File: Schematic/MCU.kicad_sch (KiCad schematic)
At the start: 0 parts

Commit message: Started to work on the BOM
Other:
- sheet ESP32 ports: added none; removed BMP_INT, GPS_RX, GPS_TX, IMU_INT, IMU_nRESET
- sheet External 40 Pin Header ports: added none; removed SENSOR_P3V3
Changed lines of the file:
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@@
-	(wire
-		(pts
-			(xy 228.6 43.18) (xy 248.92 43.18)
-		)
-		(stroke
-			(width 0)
-			(type default)
-		)
-	)
 	(wire
 		(pts
@@
 	(wire
 		(pts
-			(xy 165.1 40.64) (xy 185.42 40.64)
-		)
-		(stroke
-			(width 0)
-			(type default)
-		)
-	)
-	(wire
-		(pts
-			(xy 165.1 44.45) (xy 185.42 44.45)
+			(xy 168.91 40.64) (xy 185.42 40.64)
 		)
 		(stroke
@@
 	(wire
 		(pts
-			(xy 165.1 72.39) (xy 185.42 72.39)
-		)
-		(stroke
-			(width 0)
-			(type default)
-		)
-	)
-	(wire
-		(pts
 			(xy 165.1 60.96) (xy 185.42 60.96)
 		)
@@
 	(wire
 		(pts
-			(xy 165.1 82.55) (xy 185.42 82.55)
-		)
-		(stroke
-			(width 0)
-			(type default)
-		)
-	)
-	(wire
-		(pts
 			(xy 165.1 53.34) (xy 185.42 53.34)
 		)
@@
 	(wire
 		(pts
-			(xy 58.42 92.71) (xy 82.55 92.71)
-		)
-		(stroke
-			(width 0)
-			(type default)
-		)
-	)
-	(wire
-		(pts
 			(xy 119.38 45.72) (xy 139.7 45.72)
 		)
@@
 		(pts
 			(xy 228.6 45.72) (xy 248.92 45.72)
-		)
-		(stroke
-			(width 0)
-			(type default)
-		)
-	)
-	(wire
-		(pts
-			(xy 165.1 46.99) (xy 185.42 46.99)
 		)
 		(stroke
@@
 		)
 	)
-	(label "IMU_INT"
-		(at 165.1 72.39 0)
-		(effects
-			(font
-				(size 1.27 1.27)
-			)
-			(justify left bottom)
-		)
-	)
 	(label "IO_RST"
 		(at 248.92 45.72 180)
@@
 		)
 	)
-	(label "GPS_RX"
-		(at 165.1 44.45 0)
-		(effects
-			(font
-				(size 1.27 1.27)
-			)
-			(justify left bottom)
-		)
-	)
-	(label "BMP_INT"
-		(at 165.1 82.55 0)
-		(effects
-			(font
-				(size 1.27 1.27)
-			)
-			(justify left bottom)
-		)
-	)
 	(label "MOTOR_PH_DATA"
 		(at 165.1 91.44 0)
@@
 		)
 	)
-	(label "IMU_nRESET"
-		(at 248.92 43.18 180)
-		(effects
-			(font
-				(size 1.27 1.27)
-			)
-			(justify right bottom)
-		)
-	)
 	(label "I2C_SDA"
 		(at 62.23 105.41 0)
@@
 		)
 	)
-	(label "GPS_TX"
-		(at 165.1 46.99 0)
-		(effects
-			(font
-				(size 1.27 1.27)
-			)
-			(justify left bottom)
-		)
-	)
 	(label "SPI_SDO"
 		(at 62.23 115.57 0)
@@
 	)
 	(label "SENSOR_P3V3"
-		(at 165.1 40.64 0)
+		(at 168.91 40.64 0)
 		(effects
 			(font
@@
 			)
 			(justify right bottom)
-		)
-	)
-	(label "SENSOR_P3V3"
-		(at 62.23 92.71 0)
-		(effects
-			(font
-				(size 1.27 1.27)
-			)
-			(justify left bottom)
 		)
 	)
@@
 		)
 	)
-	(hierarchical_label "SENSOR_P3V3"
-		(shape input)
-		(at 58.42 92.71 180)
-		(effects
-			(font
-				(size 1.27 1.27)
-			)
-			(justify right)
-		)
-	)
 	(hierarchical_label "ENCODER_SEL2"
 		(shape output)
@@
 		(shape input)
 		(at 58.42 120.65 180)
+		(effects
+			(font
+				(size 1.27 1.27)
+			)
+			(justify right)
+		)
+	)
+	(hierarchical_label "SENSOR_P3V3"
+		(shape input)
+		(at 168.91 40.64 180)
 		(effects
 			(font
@@
 		(size 38.1 54.61)
 		(exclude_from_sim no)
-		(in_bom yes)
-		(on_board yes)
-		(dnp no)
+		(in_bom no)
+		(on_board no)
+		(dnp yes)
 		(fields_autoplaced yes)
 		(stroke
@@
 				)
 				(justify right)
-			)
-		)
-		(pin "SENSOR_P3V3" input
-			(at 82.55 92.71 180)
-			(effects
-				(font
-					(size 1.27 1.27)
-				)
-				(justify left)
 			)
 		)
@@
 			)
 		)
-		(pin "IMU_nRESET" output
-			(at 228.6 43.18 0)
-			(effects
-				(font
-					(size 1.27 1.27)
-				)
-				(justify right)
-			)
-		)
-		(pin "BMP_INT" input
-			(at 185.42 82.55 180)
-			(effects
-				(font
-					(size 1.27 1.27)
-				)
-				(justify left)
-			)
-		)
 		(pin "ENCODER_SEL1" output
 			(at 228.6 57.15 0)
@@
 			)
 		)
-		(pin "GPS_RX" input
-			(at 185.42 44.45 180)
-			(effects
-				(font
-					(size 1.27 1.27)
-				)
-				(justify left)
-			)
-		)
-		(pin "GPS_TX" output
-			(at 185.42 46.99 180)
-			(effects
-				(font
-					(size 1.27 1.27)
-				)
-				(justify left)
-			)
-		)
 		(pin "I2C_SCL" output
 			(at 185.42 50.8 180)
@@
 			(effects
 				(font
-					(size 1.27 1.27)
-				)
-				(justify left)
-			)
-		)
-		(pin "IMU_INT" input
-			(at 185.42 72.39 180)
-			(effects
-				(font

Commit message: Massive pivit, simplification
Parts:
- added C1, C13, C20, C23, C25, C26, C27, C28, C29, C30, C9: 100n, symbol Device:C
- added C10, C11, C18, C4: 100n, Capacitor_SMD:C_1206_3216Metric_Pad1.33x1.80mm_HandSolder, symbol Device:C
- added C12: 470n, Capacitor_SMD:C_0805_2012Metric_Pad1.18x1.45mm_HandSolder, symbol Device:C
- added C14, C15: 10p, symbol Device:C
- added C16, C2, C3: 4u7, Capacitor_SMD:C_1206_3216Metric_Pad1.33x1.80mm_HandSolder, symbol Device:C
- added C17, C22: 1u, symbol Device:C
- added C19, C21: 2u2, symbol Device:C
- added C24: 4u7, symbol Device:C
- added C31, C32: 12p, symbol Device:C
- added C5, C6, C7, C8: 10n, Capacitor_SMD:C_1206_3216Metric_Pad1.33x1.80mm_HandSolder, symbol Device:C
- added D1, D2, D3, D4, D7: 82306050029, 82306050029:WESURGE_0603134, symbol 82306050029:82306050029
- added D5: BLUE, ASMM-CR03-BU802:LEDM3528X210N, symbol PCM_SL_Devices:LED
- added D6: RED, ASMM-CR03-BU802:LEDM3528X210N, symbol PCM_SL_Devices:LED
- added FB1: 21R, symbol Device:FerriteBead_Small
- added FB2: 1k, symbol Device:FerriteBead_Small
- added J7: USB_C_Receptacle_USB2.0_14P, symbol Connector:USB_C_Receptacle_USB2.0_14P
- added J8: Conn_01x04, symbol Connector_Generic:Conn_01x04
- added NT1: NetTie_2, symbol Device:NetTie_2
- added Q1: PDTC114ET,215, PDTC114ET,215:SOT95P230X110-3N, symbol PDTC114ET,215:PDTC114ET,215
- added R1: 100k, symbol Device:R
- added R10, R13, R5: 330R, symbol Device:R
- added R11, R12: 22R, symbol Device:R
- added R2, R3: 5k1, symbol Device:R
- added R4, R7: 1k5, symbol Device:R
- added R6: 500R, symbol Device:R
- added R8: 10k, symbol Device:R
- added R9: 0R, symbol Device:R
- added SW3, SW4, SW5: SW_MEC_5E, T6VJ11GQR:T6VJ11GQR, symbol Switch:SW_MEC_5E
- added TP12, TP13, TP14, TP15, TP16, TP17, TP18: TestPoint, symbol Connector:TestPoint
- added U1: MAX809TEUR+T, MAX809TEUR+T:SOT95P237X112-3N, symbol MAX809TEUR+T:MAX809TEUR+T
- added U2: TVS2200DRV, symbol Power_Protection:TVS2200DRV
- added U3: TPS2115ADRBT, symbol TPS2115ADRBT:TPS2115ADRBT
- added U4: LM3940ISX-3.3/NOPB, symbol LM3940ISX-3-3-NOPB:LM3940ISX-3.3_NOPB
- added U5: STM32H743VIT6, Package_QFP:LQFP-100_14x14mm_P0.5mm, symbol MCU_ST_STM32H7:STM32H743VITx
- added Y1: 25M 10pF, symbol Device:Crystal_Small
- added Y2: 32.768k 7pF, symbol Device:Crystal_Small
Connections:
- net MCU_VBUS: now also C11.1, C2.2, C3.2, C4.2, FB1.2, TP12.1, U3.8 (IN1)
- net USB_C_N: now also D2.1 (A1), J7.A7 (D-), J7.B7 (D-), TP15.1
- net USB_C_P: now also D3.1 (A1), J7.A6 (D+), J7.B6 (D+), TP16.1
- new net: R1.1, R4.1, U1.2 (~{RESET})
- new net: C14.2, U5.12 (PH0), Y1.2
- new net: J8.3 (Pin_3), R12.2
- new net: C15.2, U5.13 (PH1), Y1.1
- new net: C5.1, C6.1, C7.1, C8.1, FB1.1, J7.A4 (VBUS), J7.A9 (VBUS), J7.B4 (VBUS), J7.B9 (VBUS), U2.4 (IN), U2.5 (IN), U2.6 (IN)
- new net: C32.1, U5.9 (PC15), Y2.1
- new net: C31.1, U5.8 (PC14), Y2.2
- new net: D5.1, Q1.3 (C)
- new net: D5.2, R7.2
- new net: J8.2 (Pin_2), R11.2
- new net: Q1.1 (B), U5.2 (PE3)
- new net: C19.1, U5.48 (VCAP)
- new net: R13.1, U5.7 (PC13)
- new net: C21.1, U5.73 (VCAP)
- new net: R6.1, U3.4 (ILIM)
- new net: D6.2, R10.2
- new net: C12.1, TP17.1, U3.7 (OUT), U4.1 (IN)
- new net: D7.1 (A1), R13.2, SW5.1, SW5.2
- new net BOOT0: D1.1 (A1), R8.2, SW3.1, SW3.2, U5.94 (BOOT0)
- new net C_CC1: J7.A5 (CC1), R2.1, TP13.1
- new net C_CC2: J7.B5 (CC2), R3.1, TP14.1
- new net GND: C1.2, C10.2, C11.2, C12.2, C13.1, C14.1, C15.1, C16.2, C17.2, C18.2, C19.2, C2.1, C20.2, C21.2, C22.2, C23.2, C24.2, C25.2, C26.2, C27.2, C28.2, C29.2, C3.1, C30.2, C31.2, C32.2, C4.1, C5.2, C6.2, C7.2, C8.2, C9.2, D1.2 (A2), D2.2 (A2), D3.2 (A2), D4.2 (A2), D6.1, D7.2 (A2), J7.A1 (GND), J7.A12 (GND), J7.B1 (GND), J7.B12 (GND), J7.S1 (SHIELD), J8.4 (Pin_4), NT1.1, Q1.2 (E), R1.2, R2.2, R3.2, R6.2, R8.1, SW4.3 (K), SW4.4 (A), U1.1 (GND), U2.1 (GND), U2.2 (GND), U2.3 (GND), U2.7 (GND), U3.3 (D1), U3.5 (GND), U3.9 (EPAD), U4.2 (GND), U5.10 (VSS), U5.26 (VSS), U5.49 (VSS), U5.74 (VSS), U5.99 (VSS)
- new net MCU_P3V3: C1.1, C16.1, C18.1, C24.1, C25.1, C26.1, C27.1, C28.1, C29.1, C30.1, FB2.1, J8.1 (Pin_1), R10.1, R7.1, SW3.3 (K), SW3.4 (A), SW5.3 (K), SW5.4 (A), TP18.1, U1.3 (VCC), U4.3 (OUT), U5.100 (VDD), U5.11 (VDD), U5.27 (VDD), U5.50 (VDD), U5.6 (VBAT), U5.75 (VDD)
- new net NRST: C13.2, D4.1 (A1), R4.2, SW4.1, SW4.2, U5.14 (NRST)
- new net P5V0: C10.1, U3.6 (IN2)
- new net SWCLK: R12.1, U5.76 (PA14)
- new net SWDIO: R11.1, U5.72 (PA13)
- new net SYS_RESET: C9.1, R5.2
- new net VDDA: C22.1, C23.1, FB2.2, R9.1, U5.21 (VDDA)
- new net VREF+: C17.1, C20.1, R9.2, U5.20 (VREF+)
- new net VSSA: NT1.2, U5.19 (VSSA)
- no-connect marks 0 -> 3
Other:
- removed sheet ESP32
- removed sheet External 40 Pin Header
- removed sheet MCU USB-C
- note added: "*** MAKE MORE THAN ONE AMP ***"
- note added: "100MHz"
- note added: "3V3 Line"
- note added: "3V3 Line 1A LDO"
- note added: "500/1A = 500"
- note added: "Auto-Switching Mode"
- note added: "Boot & Reset Buttons"
- note added: "Boot Switch"
- note added: "JTAG"
- note added: "Reset Switch"
- note added: "USB-C"
- note added: "User Button"

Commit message: now need 6V Line
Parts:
- removed C1, C13, C20, C23, C25, C26, C27, C28, C29, C30, C9: 100n, symbol Device:C
- removed C10, C11, C18, C4: 100n, Capacitor_SMD:C_1206_3216Metric_Pad1.33x1.80mm_HandSolder, symbol Device:C
- removed C12: 470n, Capacitor_SMD:C_0805_2012Metric_Pad1.18x1.45mm_HandSolder, symbol Device:C
- removed C14, C15: 10p, symbol Device:C
- removed C16, C2, C3: 4u7, Capacitor_SMD:C_1206_3216Metric_Pad1.33x1.80mm_HandSolder, symbol Device:C
- removed C17, C22: 1u, symbol Device:C
- removed C19, C21: 2u2, symbol Device:C
- removed C24: 4u7, symbol Device:C
- removed C31, C32: 12p, symbol Device:C
- removed C5, C6, C7, C8: 10n, Capacitor_SMD:C_1206_3216Metric_Pad1.33x1.80mm_HandSolder, symbol Device:C
- removed D1, D2, D3, D4, D7: 82306050029, 82306050029:WESURGE_0603134, symbol 82306050029:82306050029
- removed D5: BLUE, ASMM-CR03-BU802:LEDM3528X210N, symbol PCM_SL_Devices:LED
- removed D6: RED, ASMM-CR03-BU802:LEDM3528X210N, symbol PCM_SL_Devices:LED
- removed FB1: 21R, symbol Device:FerriteBead_Small
- removed FB2: 1k, symbol Device:FerriteBead_Small
- removed J7: USB_C_Receptacle_USB2.0_14P, symbol Connector:USB_C_Receptacle_USB2.0_14P
- removed J8: Conn_01x04, symbol Connector_Generic:Conn_01x04
- removed NT1: NetTie_2, symbol Device:NetTie_2
- removed Q1: PDTC114ET,215, PDTC114ET,215:SOT95P230X110-3N, symbol PDTC114ET,215:PDTC114ET,215
- removed R1: 100k, symbol Device:R
- removed R10, R13, R5: 330R, symbol Device:R
- removed R11, R12: 22R, symbol Device:R
- removed R2, R3: 5k1, symbol Device:R
- removed R4, R7: 1k5, symbol Device:R
- removed R6: 500R, symbol Device:R
- removed R8: 10k, symbol Device:R
- removed R9: 0R, symbol Device:R
- removed SW3, SW4, SW5: SW_MEC_5E, T6VJ11GQR:T6VJ11GQR, symbol Switch:SW_MEC_5E
- removed TP12, TP13, TP14, TP15, TP16, TP17, TP18: TestPoint, symbol Connector:TestPoint
- removed U1: MAX809TEUR+T, MAX809TEUR+T:SOT95P237X112-3N, symbol MAX809TEUR+T:MAX809TEUR+T
- removed U2: TVS2200DRV, symbol Power_Protection:TVS2200DRV
- removed U3: TPS2115ADRBT, symbol TPS2115ADRBT:TPS2115ADRBT
- removed U4: LM3940ISX-3.3/NOPB, symbol LM3940ISX-3-3-NOPB:LM3940ISX-3.3_NOPB
- removed U5: STM32H743VIT6, Package_QFP:LQFP-100_14x14mm_P0.5mm, symbol MCU_ST_STM32H7:STM32H743VITx
- removed Y1: 25M 10pF, symbol Device:Crystal_Small
- removed Y2: 32.768k 7pF, symbol Device:Crystal_Small
- added J14, J15: Conn_02x20_Odd_Even, symbol Connector_Generic:Conn_02x20_Odd_Even
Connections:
- net GND: now also J14.14 (Pin_14), J14.20 (Pin_20), J14.25 (Pin_25), J14.30 (Pin_30), J14.34 (Pin_34), J14.39 (Pin_39), J14.6 (Pin_6), J14.9 (Pin_9), J15.14 (Pin_14), J15.20 (Pin_20), J15.25 (Pin_25), J15.30 (Pin_30), J15.34 (Pin_34), J15.39 (Pin_39), J15.6 (Pin_6), J15.9 (Pin_9)
- net MCU_P3V3: now also J14.1 (Pin_1), J14.17 (Pin_17), J15.1 (Pin_1), J15.17 (Pin_17)
- new net 5V: J14.2 (Pin_2), J14.4 (Pin_4), J15.2 (Pin_2), J15.4 (Pin_4)
- new net ENCODER1_LFLAG/: J14.16 (Pin_16), J15.16 (Pin_16)
- new net ENCODER1_nCS: J14.15 (Pin_15), J15.15 (Pin_15)
- new net ENCODER2_LFLAG/: J14.18 (Pin_18), J15.18 (Pin_18)
- new net ENCODER2_nCS: J14.29 (Pin_29), J15.29 (Pin_29)
- new net GPCLK0: J14.7 (Pin_7), J15.7 (Pin_7)
- new net ID_SD: J14.27 (Pin_27), J15.27 (Pin_27)
- new net IO1: J14.28 (Pin_28), J15.28 (Pin_28)
- new net IO16: J14.36 (Pin_36), J15.36 (Pin_36)
- new net IO20: J14.38 (Pin_38), J15.38 (Pin_38)
- new net IO21: J14.40 (Pin_40), J15.40 (Pin_40)
- new net IO7: J14.26 (Pin_26), J15.26 (Pin_26)
- new net MOTOR1_EN_IN1: J14.32 (Pin_32), J15.32 (Pin_32)
- new net MOTOR1_PH_IN2: J14.31 (Pin_31), J15.31 (Pin_31)
- new net MOTOR1_nCS: J14.11 (Pin_11), J15.11 (Pin_11)
- new net MOTOR1_nFAULT: J14.22 (Pin_22), J15.22 (Pin_22)
- new net MOTOR2_EN_IN1: J14.33 (Pin_33), J15.33 (Pin_33)
- new net MOTOR2_PH_IN2: J14.37 (Pin_37), J15.37 (Pin_37)
- new net MOTOR2_nCS: J14.13 (Pin_13), J15.13 (Pin_13)
- new net MOTOR2_nFAULT: J14.24 (Pin_24), J15.24 (Pin_24)
- new net PCM_CLK: J14.12 (Pin_12), J15.12 (Pin_12)
- new net PCM_FS: J14.35 (Pin_35), J15.35 (Pin_35)
- new net RXD: J14.10 (Pin_10), J15.10 (Pin_10)
- new net SCL: J14.5 (Pin_5), J15.5 (Pin_5)
- new net SDA: J14.3 (Pin_3), J15.3 (Pin_3)
- new net SPI_SCLK: J14.23 (Pin_23), J15.23 (Pin_23)
- new net SPI_SDI: J14.19 (Pin_19), J15.19 (Pin_19)
- new net SPI_SDO: J14.21 (Pin_21), J15.21 (Pin_21)
- new net TXD: J14.8 (Pin_8), J15.8 (Pin_8)
- no-connect marks 3 -> 0
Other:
- note added: "FEMALE"
- note added: "MALE"
- note removed: "*** MAKE MORE THAN ONE AMP ***"
- note removed: "100MHz"
- note removed: "3V3 Line"
- note removed: "3V3 Line 1A LDO"
- note removed: "500/1A = 500"
- note removed: "Auto-Switching Mode"
- note removed: "Boot & Reset Buttons"
- note removed: "Boot Switch"
- note removed: "JTAG"
- note removed: "Reset Switch"
- note removed: "USB-C"
- note removed: "User Button"

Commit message: bom progress
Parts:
- J14: footprint (none) -> 7-534206-0:SHDR40W69P254_2X20_5080X503X813P
- J15: footprint (none) -> Connector_PinHeader_2.54mm:PinHeader_2x20_P2.54mm_Vertical
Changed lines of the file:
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@@
 			)
 		)
-		(property "Footprint" ""
+		(property "Footprint" "Connector_PinHeader_2.54mm:PinHeader_2x20_P2.54mm_Vertical"
 			(at 196.85 96.52 0)
 			(effects
@@
 			)
 		)
-		(property "Footprint" ""
+		(property "Footprint" "7-534206-0:SHDR40W69P254_2X20_5080X503X813P"
 			(at 96.52 96.52 0)
 			(effects

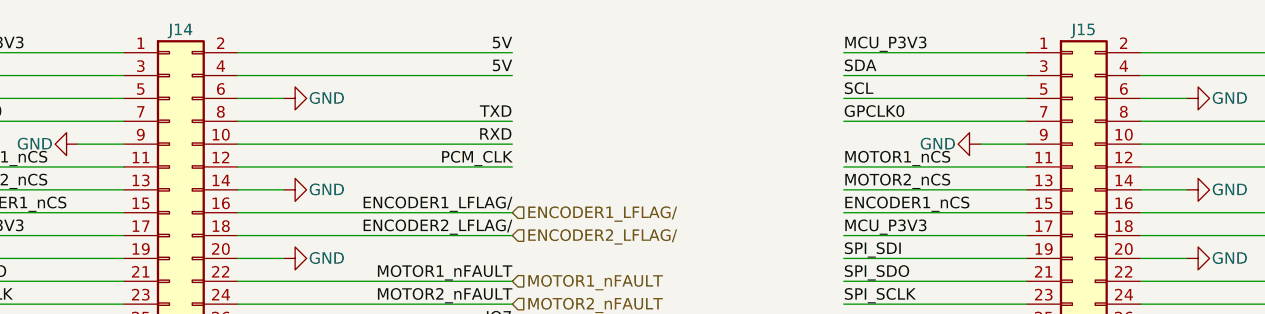
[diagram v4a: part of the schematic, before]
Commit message: added test points and fet
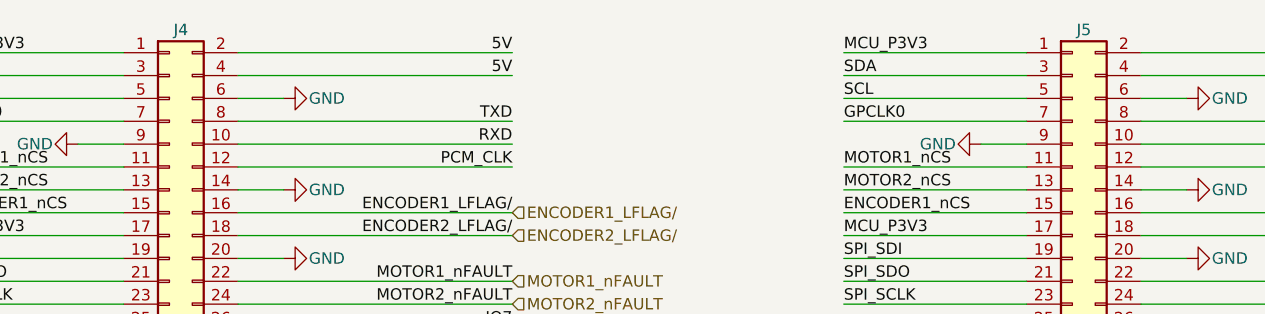
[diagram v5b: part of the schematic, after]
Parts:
- renumbered J14 to J4, J15 to J5
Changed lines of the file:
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@@
 		(on_board yes)
 		(dnp no)
-		(property "Reference" "#PWR065"
+		(property "Reference" "#PWR05"
 			(at 80.01 121.92 0)
 			(effects
@@
 			(project "STAR"
 				(path "/fc8533bc-25dd-4c20-9b4c-ffebebd6739b/f27ff2e9-3317-49a4-9819-b00013085e8b"
-					(reference "#PWR065")
+					(reference "#PWR05")
 					(unit 1)
 				)
@@
 		(on_board yes)
 		(dnp no)
-		(property "Reference" "#PWR070"
+		(property "Reference" "#PWR012"
 			(at 180.34 104.14 0)
 			(effects
@@
 			(project "STAR"
 				(path "/fc8533bc-25dd-4c20-9b4c-ffebebd6739b/f27ff2e9-3317-49a4-9819-b00013085e8b"
-					(reference "#PWR070")
+					(reference "#PWR012")
 					(unit 1)
 				)
@@
 		(on_board yes)
 		(dnp no)
-		(property "Reference" "#PWR068"
+		(property "Reference" "#PWR08"
 			(at 115.57 96.52 0)
 			(effects
@@
 			(project "STAR"
 				(path "/fc8533bc-25dd-4c20-9b4c-ffebebd6739b/f27ff2e9-3317-49a4-9819-b00013085e8b"
-					(reference "#PWR068")
+					(reference "#PWR08")
 					(unit 1)
 				)
@@
 		(on_board yes)
 		(dnp no)
-		(property "Reference" "J15"
+		(property "Reference" "J5"
 			(at 198.12 71.12 0)
 			(effects
@@
 			(project "STAR"
 				(path "/fc8533bc-25dd-4c20-9b4c-ffebebd6739b/f27ff2e9-3317-49a4-9819-b00013085e8b"
-					(reference "J15")
+					(reference "J5")
 					(unit 1)
 				)
@@
 		(on_board yes)
 		(dnp no)
-		(property "Reference" "#PWR062"
+		(property "Reference" "#PWR07"
 			(at 115.57 88.9 0)
 			(effects
@@
 			(project "STAR"
 				(path "/fc8533bc-25dd-4c20-9b4c-ffebebd6739b/f27ff2e9-3317-49a4-9819-b00013085e8b"
-					(reference "#PWR062")
+					(reference "#PWR07")
 					(unit 1)
 				)
@@
 		(on_board yes)
 		(dnp no)
-		(property "Reference" "#PWR064"
+		(property "Reference" "#PWR04"
 			(at 80.01 104.14 0)
 			(effects
@@
 			(project "STAR"
 				(path "/fc8533bc-25dd-4c20-9b4c-ffebebd6739b/f27ff2e9-3317-49a4-9819-b00013085e8b"
-					(reference "#PWR064")
+					(reference "#PWR04")
 					(unit 1)
 				)
@@
 		(on_board yes)
 		(dnp no)
-		(property "Reference" "#PWR066"
+		(property "Reference" "#PWR010"
 			(at 115.57 114.3 0)
 			(effects
@@
 			(project "STAR"
 				(path "/fc8533bc-25dd-4c20-9b4c-ffebebd6739b/f27ff2e9-3317-49a4-9819-b00013085e8b"
-					(reference "#PWR066")
+					(reference "#PWR010")
 					(unit 1)
 				)
@@
 		(on_board yes)
 		(dnp no)
-		(property "Reference" "J14"
+		(property "Reference" "J4"
 			(at 97.79 71.12 0)
 			(effects
@@
 			(project ""
 				(path "/fc8533bc-25dd-4c20-9b4c-ffebebd6739b/f27ff2e9-3317-49a4-9819-b00013085e8b"
-					(reference "J14")
+					(reference "J4")
 					(unit 1)
 				)
@@
 		(on_board yes)
 		(dnp no)
-		(property "Reference" "#PWR076"
+		(property "Reference" "#PWR018"
 			(at 215.9 114.3 0)
 			(effects
@@
 			(project "STAR"
 				(path "/fc8533bc-25dd-4c20-9b4c-ffebebd6739b/f27ff2e9-3317-49a4-9819-b00013085e8b"
-					(reference "#PWR076")
+					(reference "#PWR018")
 					(unit 1)
 				)
@@
 		(on_board yes)
 		(dnp no)
-		(property "Reference" "#PWR071"
+		(property "Reference" "#PWR013"
 			(at 180.34 121.92 0)
 			(effects
@@
 			(project "STAR"
 				(path "/fc8533bc-25dd-4c20-9b4c-ffebebd6739b/f27ff2e9-3317-49a4-9819-b00013085e8b"
-					(reference "#PWR071")
+					(reference "#PWR013")
 					(unit 1)
 				)
@@
 		(on_board yes)
 		(dnp no)
-		(property "Reference" "#PWR074"
+		(property "Reference" "#PWR016"
 			(at 215.9 96.52 0)
 			(effects
@@
 			(project "STAR"
 				(path "/fc8533bc-25dd-4c20-9b4c-ffebebd6739b/f27ff2e9-3317-49a4-9819-b00013085e8b"
-					(reference "#PWR074")
+					(reference "#PWR016")
 					(unit 1)
 				)
@@
 		(on_board yes)
 		(dnp no)
-		(property "Reference" "#PWR072"
+		(property "Reference" "#PWR014"
 			(at 215.9 78.74 0)
 			(effects
@@
 			(project "STAR"
 				(path "/fc8533bc-25dd-4c20-9b4c-ffebebd6739b/f27ff2e9-3317-49a4-9819-b00013085e8b"
-					(reference "#PWR072")
+					(reference "#PWR014")
 					(unit 1)
 				)
@@
 		(on_board yes)
 		(dnp no)
-		(property "Reference" "#PWR073"
+		(property "Reference" "#PWR015"
 			(at 215.9 88.9 0)
 			(effects
@@
 			(project "STAR"
 				(path "/fc8533bc-25dd-4c20-9b4c-ffebebd6739b/f27ff2e9-3317-49a4-9819-b00013085e8b"
-					(reference "#PWR073")
+					(reference "#PWR015")
 					(unit 1)
 				)
@@
 		(on_board yes)
 		(dnp no)
-		(property "Reference" "#PWR067"
+		(property "Reference" "#PWR09"
 			(at 115.57 109.22 0)
 			(effects
@@
 			(project "STAR"
 				(path "/fc8533bc-25dd-4c20-9b4c-ffebebd6739b/f27ff2e9-3317-49a4-9819-b00013085e8b"
-					(reference "#PWR067")
+					(reference "#PWR09")
 					(unit 1)
 				)
@@
 		(on_board yes)
 		(dnp no)
-		(property "Reference" "#PWR069"
+		(property "Reference" "#PWR011"
 			(at 180.34 83.82 0)
 			(effects
@@
 			(project "STAR"
 				(path "/fc8533bc-25dd-4c20-9b4c-ffebebd6739b/f27ff2e9-3317-49a4-9819-b00013085e8b"
-					(reference "#PWR069")
+					(reference "#PWR011")
 					(unit 1)
 				)
@@
 		(on_board yes)
 		(dnp no)
-		(property "Reference" "#PWR063"
+		(property "Reference" "#PWR03"
 			(at 80.01 83.82 0)
 			(effects
@@
 			(project "STAR"
 				(path "/fc8533bc-25dd-4c20-9b4c-ffebebd6739b/f27ff2e9-3317-49a4-9819-b00013085e8b"
-					(reference "#PWR063")
+					(reference "#PWR03")
 					(unit 1)
 				)
@@
 		(on_board yes)
 		(dnp no)
-		(property "Reference" "#PWR061"
+		(property "Reference" "#PWR06"
 			(at 115.57 78.74 0)
 			(effects
@@
 			(project "STAR"
 				(path "/fc8533bc-25dd-4c20-9b4c-ffebebd6739b/f27ff2e9-3317-49a4-9819-b00013085e8b"
-					(reference "#PWR061")
+					(reference "#PWR06")
 					(unit 1)
 				)
@@
 		(on_board yes)
 		(dnp no)
-		(property "Reference" "#PWR075"
+		(property "Reference" "#PWR017"
 			(at 215.9 109.22 0)
 			(effects
@@
 			(project "STAR"
 				(path "/fc8533bc-25dd-4c20-9b4c-ffebebd6739b/f27ff2e9-3317-49a4-9819-b00013085e8b"
-					(reference "#PWR075")
-					(unit 1)
-				)
+					(reference "#PWR017")
+					(unit 1)
+				)

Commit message: need to do Qs now
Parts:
- J4: DigiKey Link (none) -> https://www.digikey.com/short/wv5bdndv; DigiKey Price per Unit (none) -> 7.03; Manufactaurer Part Number (none) -> 7-534206-0; Mouser Link (none) -> https://mou.sr/4hKjd4j; Mouser Part Number (none) -> 571-7-534206-0; Mouser Price per Unit (none) -> 6.99
- J5: now left out of the parts list
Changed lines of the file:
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@@
 		(unit 1)
 		(exclude_from_sim no)
-		(in_bom yes)
+		(in_bom no)
 		(on_board yes)
 		(dnp no)
@@
 			)
 		)
-		(property "DigiKey Link" ""
+		(property "DigiKey Link" "https://www.digikey.com/short/wv5bdndv"
 			(at 96.52 96.52 0)
 			(effects
@@
 			(at 96.52 96.52 0)
 			(effects
+				(font
+					(size 1.27 1.27)
+				)
+				(hide yes)
+			)
+		)
+		(property "DigiKey Price per Unit" "7.03"
+			(at 96.52 96.52 0)
+			(effects
+				(font
+					(size 1.27 1.27)
+				)
+				(hide yes)
+			)
+		)
+		(property "Manufactaurer Part Number" "7-534206-0"
+			(at 96.52 96.52 0)
+			(effects
+				(font
+					(size 1.27 1.27)
+				)
+				(hide yes)
+			)
+		)
+		(property "Mouser Link" "https://mou.sr/4hKjd4j"
+			(at 96.52 96.52 0)
+			(effects
+				(font
+					(size 1.27 1.27)
+				)
+				(hide yes)
+			)
+		)
+		(property "Mouser Part Number" "571-7-534206-0"
+			(at 96.52 96.52 0)
+			(effects
+				(font
+					(size 1.27 1.27)
+				)
+				(hide yes)
+			)
+		)
+		(property "Mouser Price per Unit" "6.99"
+			(at 96.52 96.52 0)
+			(effects
